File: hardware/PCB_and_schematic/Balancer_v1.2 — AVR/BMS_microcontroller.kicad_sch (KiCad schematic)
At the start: 52 parts, among them J10 RS485, J16 ICP, J2 VOLTAGE_3WIRE, J8 Conn_01x06, J9 RS485, Q23 BC817, U10 PC817, U11 LM7805_TO220, U4 TL432DBZ, U5 ADUM3211ARZ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

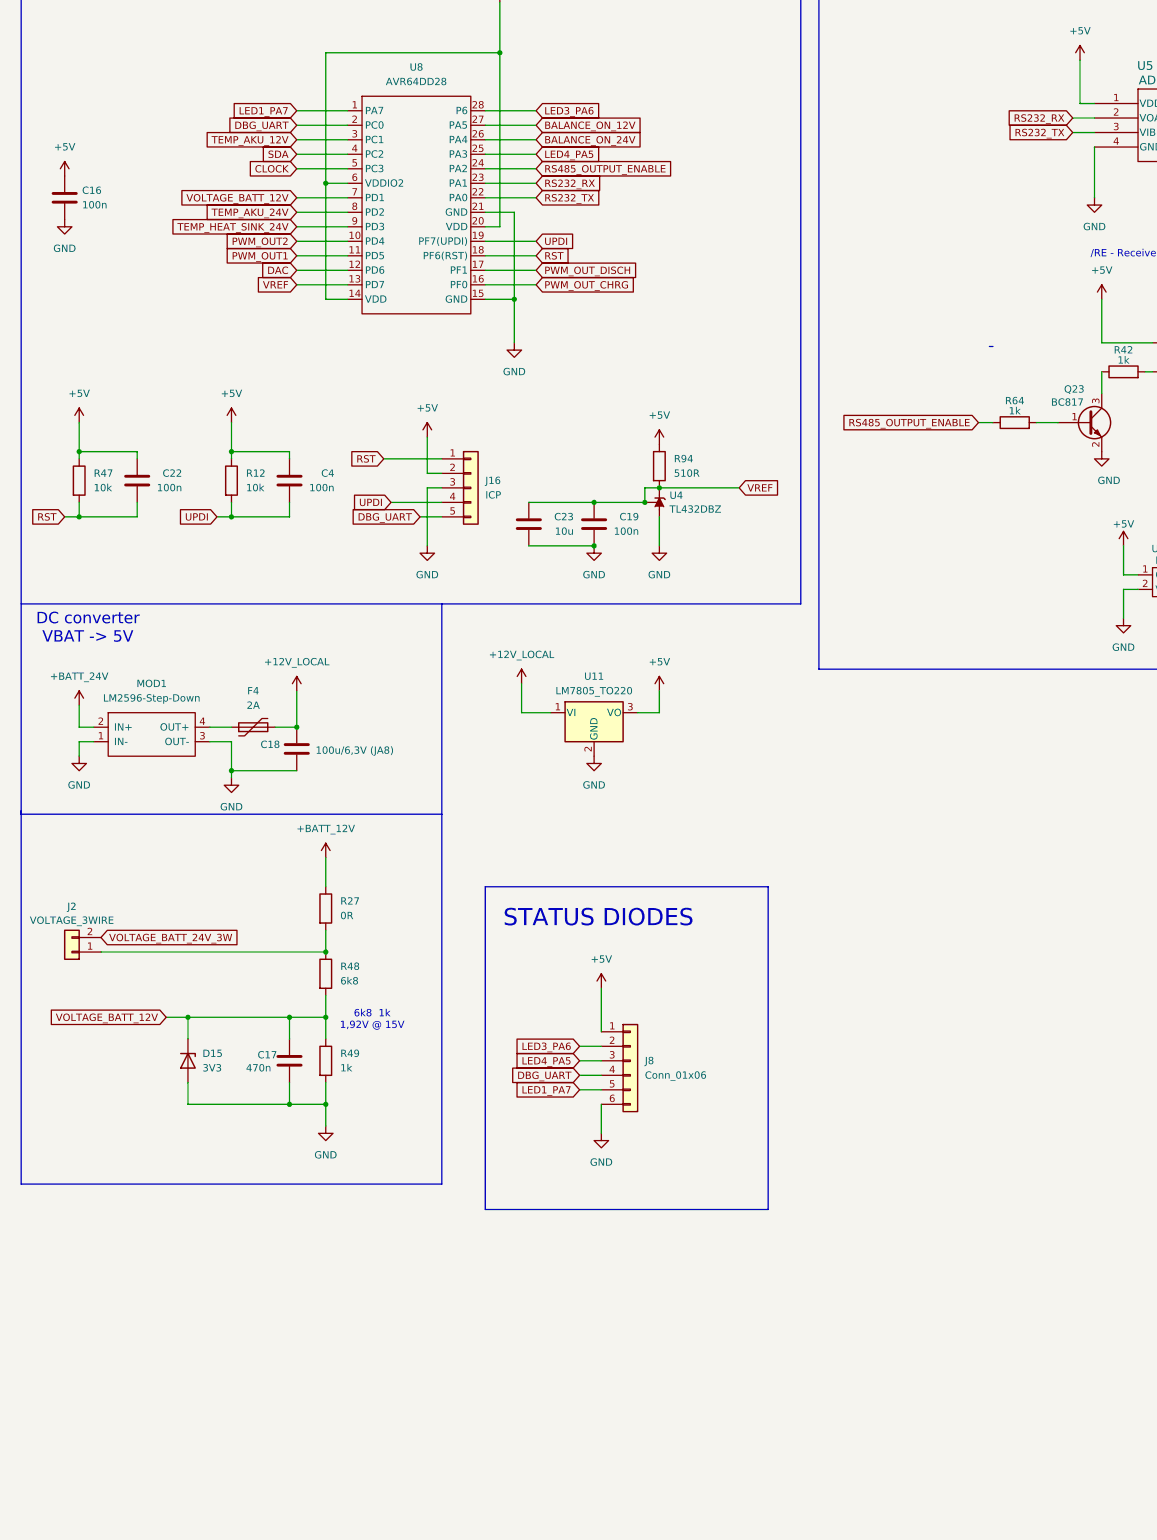
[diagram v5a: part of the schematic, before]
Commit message: update balancer pcb - add gnd vdrop opamp
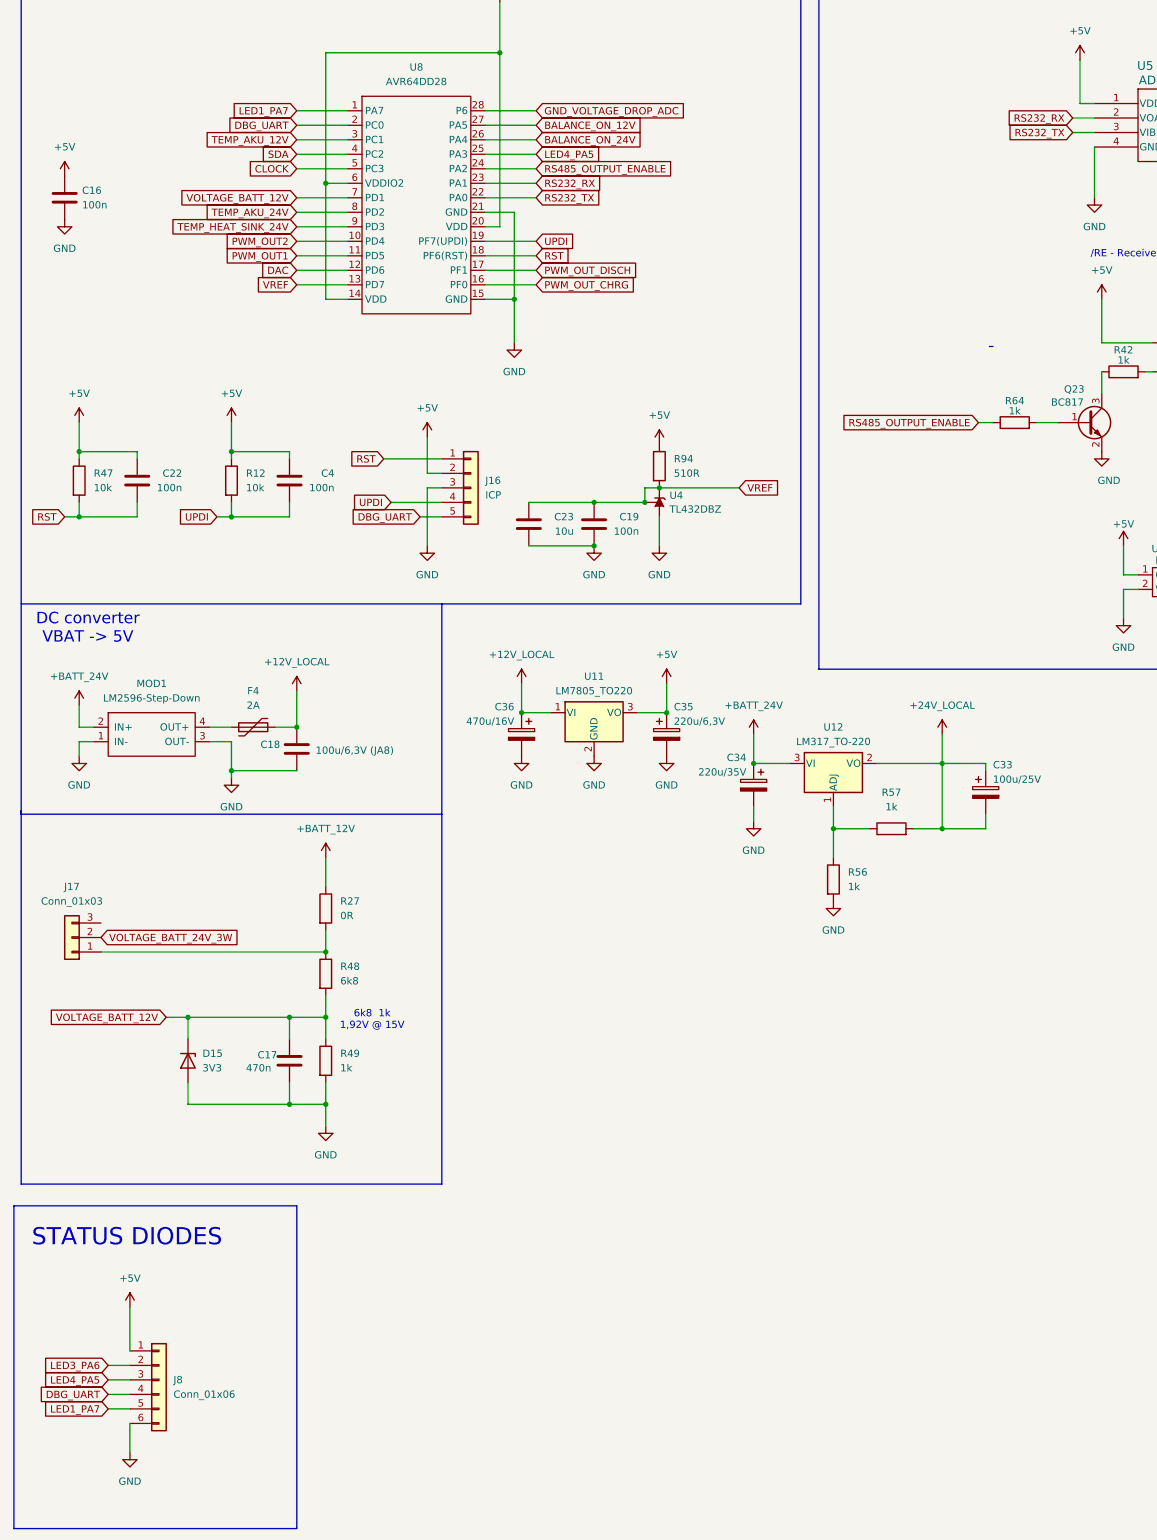
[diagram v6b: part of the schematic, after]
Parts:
- removed J2: VOLTAGE_3WIRE, Connector_JST:JST_XH_B2B-XH-A_1x02_P2.50mm_Vertical, symbol Connector_Generic:Conn_01x02
- added C33: 100u/25V, Capacitor_THT:CP_Radial_D8.0mm_P2.50mm, symbol Device:C_Polarized
- added C34: 220u/35V, Capacitor_THT:CP_Radial_D8.0mm_P2.50mm, symbol Device:C_Polarized
- added C35: 220u/6,3V, Capacitor_THT:CP_Radial_D8.0mm_P2.50mm, symbol Device:C_Polarized
- added C36: 470u/16V, Capacitor_THT:CP_Radial_D8.0mm_P2.50mm, symbol Device:C_Polarized
- added J17: Conn_01x03, symbol Connector_Generic:Conn_01x03
- added R56, R57: 1k, Resistor_SMD:R_0805_2012Metric_Pad1.20x1.40mm_HandSolder, symbol Device:R
- added U12: LM317_TO-220, Package_TO_SOT_THT:TO-220-3_Vertical, symbol Regulator_Linear:LM317_TO-220
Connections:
- net +12V_LOCAL: now also C36.1
- net +5V: now also C35.1
- net +BATT_24V: now also C34.1, U12.3 (VI)
- net GND: now also C34.2, C35.2, C36.2, R56.2
- net LED3_PA6: no longer U8.28 (P6)
- net VOLTAGE_BATT_24V_3W: now also J17.2 (Pin_2)
- net at R27.2, R48.1: now also J17.1 (Pin_1)
- new net: R56.1, R57.1, U12.1 (ADJ)
- new net +24V_LOCAL: C33.1, C33.2, R57.2, U12.2 (VO)
- new net GND_VOLTAGE_DROP_ADC: U8.28 (P6)
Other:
- moved on the sheet: J8

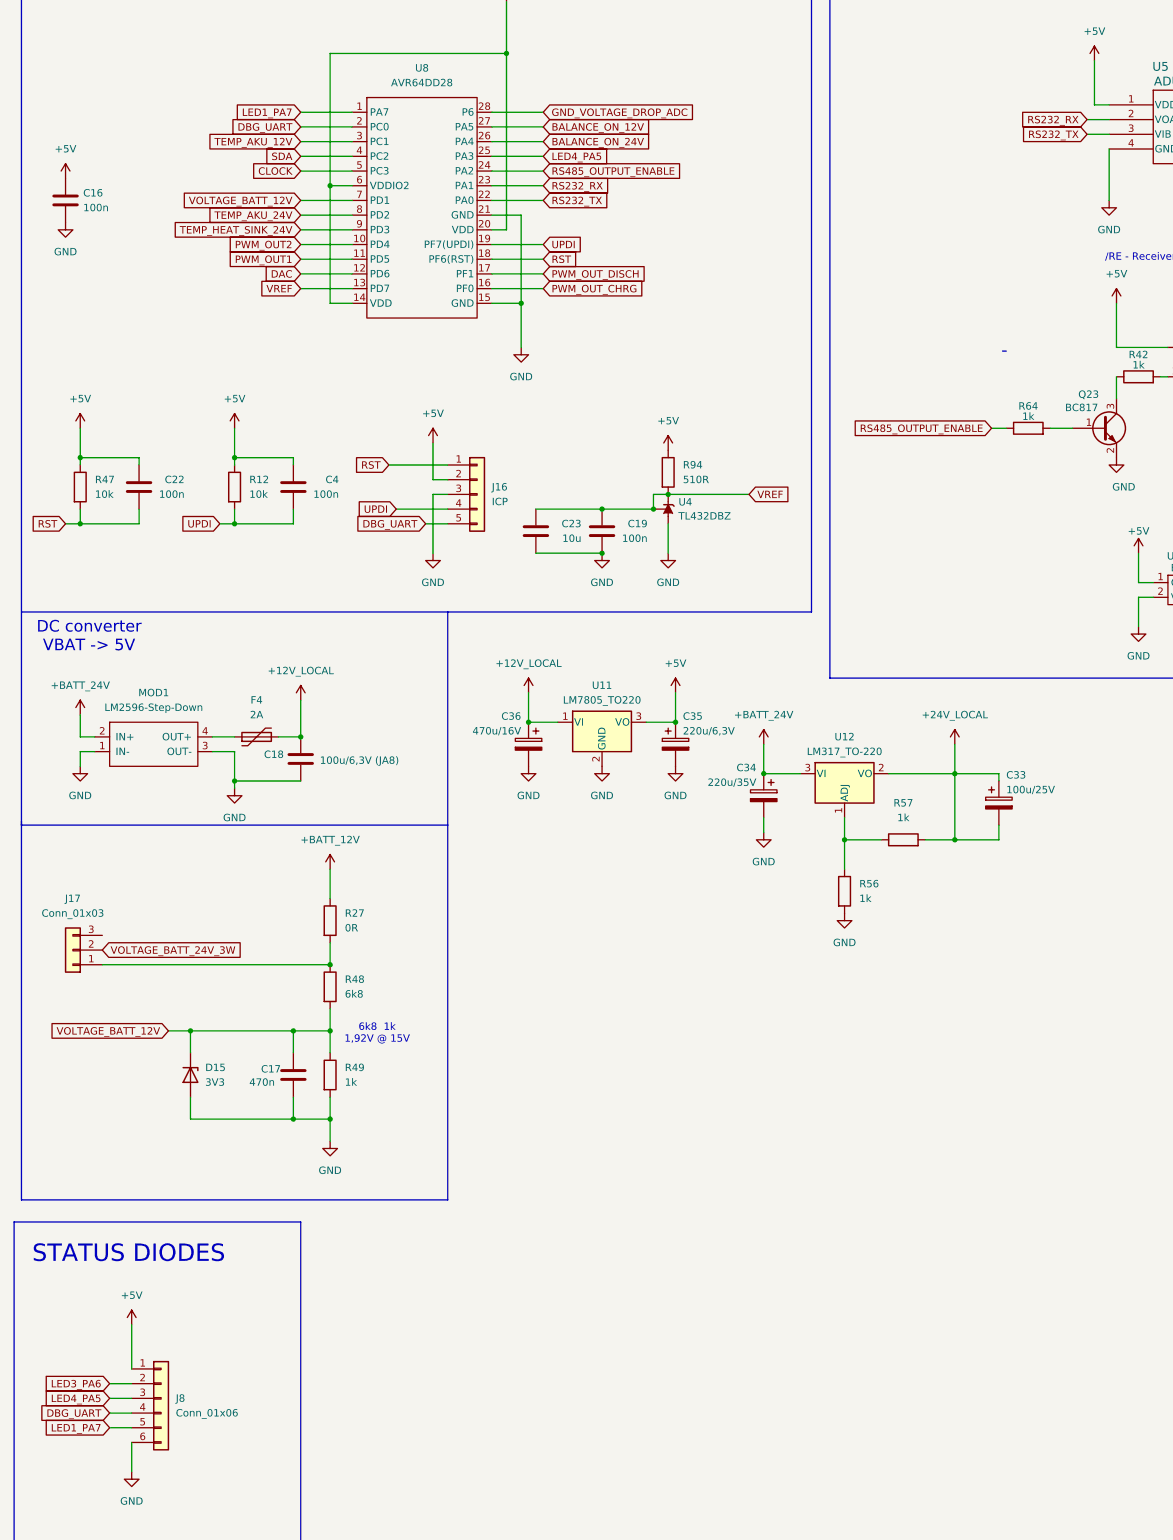
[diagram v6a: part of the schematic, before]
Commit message: Update balacer schematic - change fan drive circuit,  fix current limiter drive
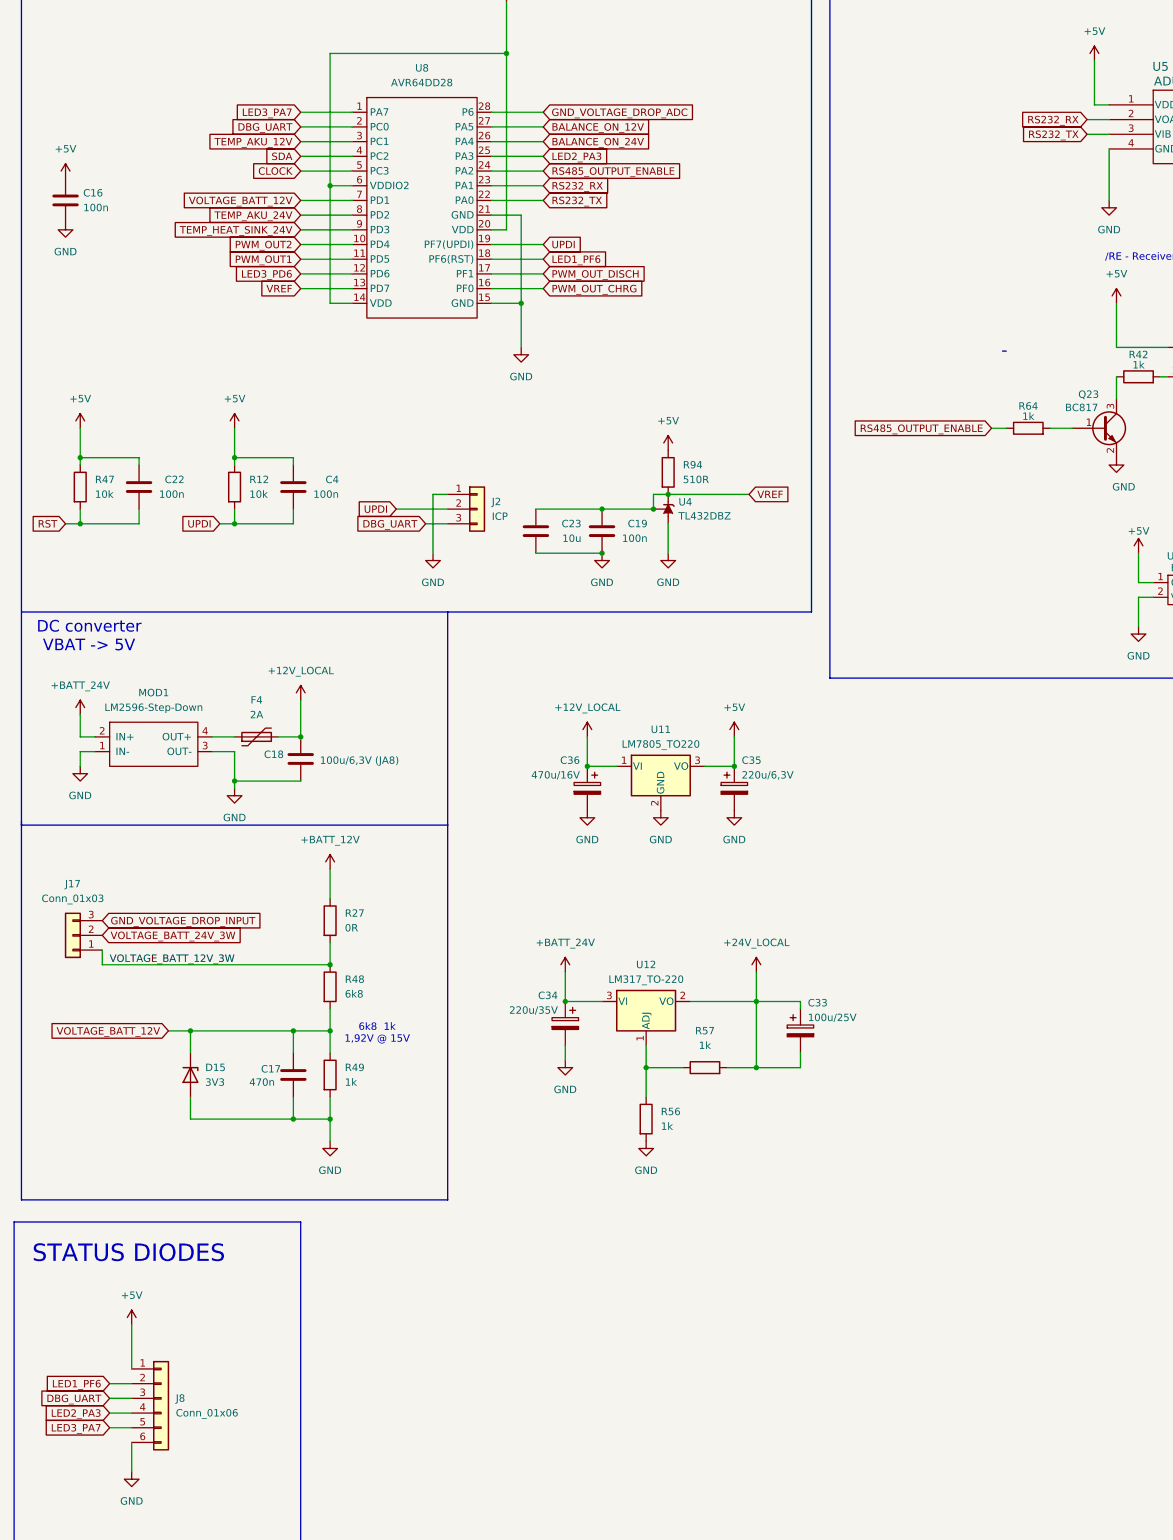
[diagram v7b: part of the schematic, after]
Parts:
- removed J16: ICP, Connector_PinHeader_2.54mm:PinHeader_1x05_P2.54mm_Vertical, symbol Connector_Generic:Conn_01x05
- added J2: ICP, symbol Connector_Generic:Conn_01x03
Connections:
- net DBG_UART: now also J8.3 (Pin_3), J2.3 (Pin_3); no longer J8.4 (Pin_4)
- net GND: now also J2.1 (Pin_1)
- net RST: no longer U8.18 (PF6(RST))
- net UPDI: now also J2.2 (Pin_2)
- net VOLTAGE_BATT_12V_3W: now reaches J17.1 (Pin_1), R27.2, R48.1
- net GND_VOLTAGE_DROP_INPUT: now reaches J17.3 (Pin_3)
- net DAC renamed LED3_PD6
- net LED1_PA7 renamed LED3_PA7
- net LED3_PA6 renamed LED1_PF6
- net LED1_PF6: now also U8.18 (PF6(RST))
- net LED4_PA5 renamed LED2_PA3
- net LED2_PA3: now also J8.4 (Pin_4); no longer J8.3 (Pin_3)
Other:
- moved on the sheet: C33, C34, C35, C36, J17, R56, R57, U11, U12
